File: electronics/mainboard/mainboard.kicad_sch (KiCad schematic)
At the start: 24 parts, among them Q1 TSM250N02CX_RFG, Q2 TSM250N02CX_RFG, SW1 SW_Push, SW10 SW_Push, SW11 SW_Push, SW12 SW_Push, SW13 SW_Push, SW14 SW_Push, SW15 SW_Push, SW2 SW_Push, SW3 SW_Push, SW4 SW_Push, SW5 SW_Push, SW6 SW_Push, SW7 SW_Push, SW8 SW_Push, SW9 SW_Push, U1 1022

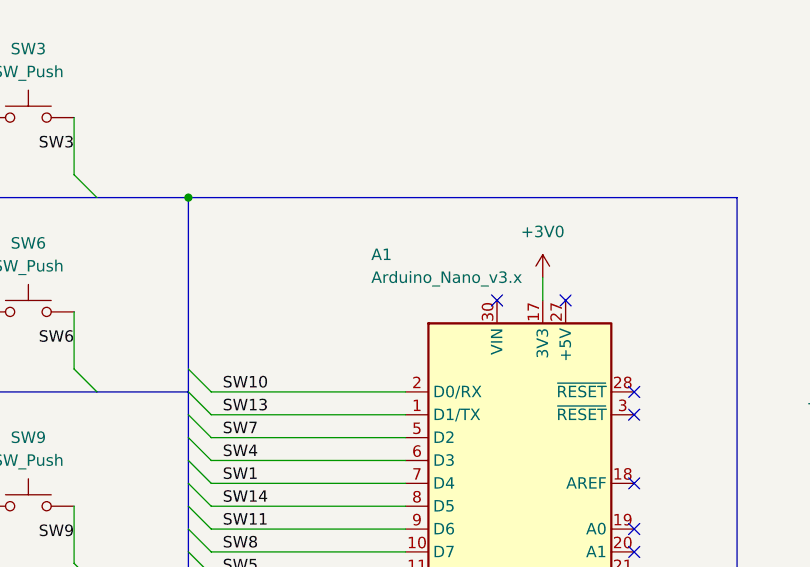
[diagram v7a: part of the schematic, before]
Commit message: clarify designator of arduino
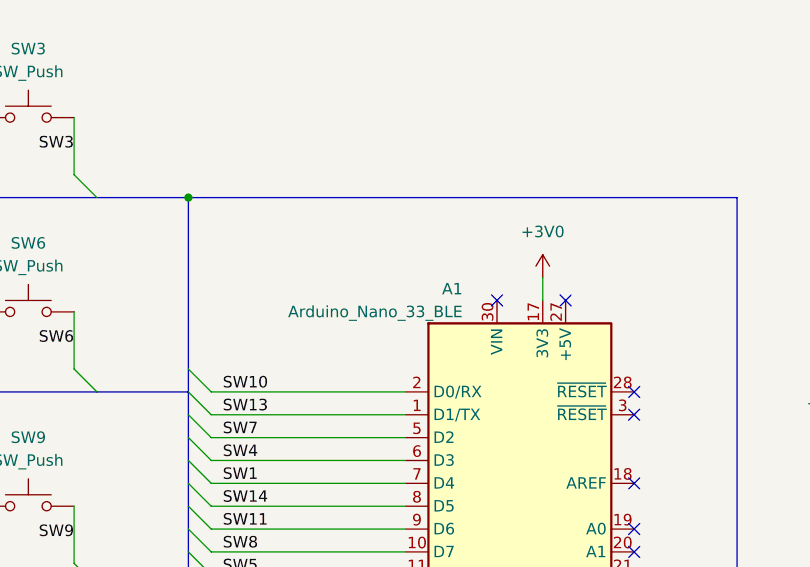
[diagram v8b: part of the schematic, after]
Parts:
- A1: value Arduino_Nano_v3.x -> Arduino_Nano_33_BLE
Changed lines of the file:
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@@
   (symbol (lib_id "MCU_Module:Arduino_Nano_v3.x") (at 222.25 93.98 0) (unit 1)
     (in_bom yes) (on_board yes)
-    (property "Reference" "A1" (id 0) (at 205.74 63.5 0)
-      (effects (font (size 1.27 1.27)) (justify left))
-    )
-    (property "Value" "Arduino_Nano_v3.x" (id 1) (at 205.74 66.04 0)
-      (effects (font (size 1.27 1.27)) (justify left))
+    (property "Reference" "A1" (id 0) (at 215.9 67.31 0)
+      (effects (font (size 1.27 1.27)) (justify right))
+    )
+    (property "Value" "Arduino_Nano_33_BLE" (id 1) (at 215.9 69.85 0)
+      (effects (font (size 1.27 1.27)) (justify right))
     )
     (property "Footprint" "Module:Arduino_Nano_WithMountingHoles" (id 2) (at 222.25 93.98 0)
@@
     )
     (path "/8fac398c-22c9-4741-a001-aab7ea92da04"
-      (reference "A1") (unit 1) (value "Arduino_Nano_v3.x") (footprint "Module:Arduino_Nano_WithMountingHoles")
+      (reference "A1") (unit 1) (value "Arduino_Nano_33_BLE") (footprint "Module:Arduino_Nano_WithMountingHoles")
     )
     (path "/cf3301c7-941c-41e4-b103-0007295da9ac"
